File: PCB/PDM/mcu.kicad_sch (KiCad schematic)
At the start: 1 part, among them U1 STM32F405RGTx

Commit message: Fuck christmas & low side section
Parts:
- removed U1: STM32F405RGTx, Package_QFP:LQFP-64_10x10mm_P0.5mm, symbol MCU_ST_STM32F4:STM32F405RGTx
- added U1: STM32L496VGTx, Package_QFP:LQFP-100_14x14mm_P0.5mm, symbol MCU_ST_STM32L4:STM32L496VGTx
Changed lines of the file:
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@@
 (kicad_sch (version 20211123) (generator eeschema)
   (paper "A4")
-  (symbol (lib_id "MCU_ST_STM32F4:STM32F405RGTx") (at 67.945 74.93 0) (unit 1)
+  (symbol (lib_id "MCU_ST_STM32L4:STM32L496VGTx") (at 75.565 105.41 0) (unit 1)
     (in_bom yes) (on_board yes) (fields_autoplaced)
-    (property "Reference" "U1" (id 0) (at 72.5044 120.65 0)
-      (effects (font (size 0.8 0.8)) (justify left))
+    (property "Reference" "U1" (id 0) (at 85.2044 173.99 0)
+      (effects (font (size 1.27 1.27)) (justify left))
     )
-    (property "Value" "STM32F405RGTx" (id 1) (at 72.5044 123.19 0)
-      (effects (font (size 0.8 0.8)) (justify left))
+    (property "Value" "STM32L496VGTx" (id 1) (at 85.2044 176.53 0)
+      (effects (font (size 1.27 1.27)) (justify left))
     )
-    (property "Footprint" "Package_QFP:LQFP-64_10x10mm_P0.5mm" (id 2) (at 52.705 118.11 0)
+    (property "Footprint" "Package_QFP:LQFP-100_14x14mm_P0.5mm" (id 2) (at 57.785 171.45 0)
       (effects (font (size 1.27 1.27)) (justify right) hide)
     )
-    (property "Datasheet" "http://www.st.com/st-web-ui/static/active/en/resource/technical/document/datasheet/DM00037051.pdf" (id 3) (at 67.945 74.93 0)
+    (property "Datasheet" "http://www.st.com/st-web-ui/static/active/en/resource/technical/document/datasheet/DM00284211.pdf" (id 3) (at 75.565 105.41 0)
       (effects (font (size 1.27 1.27)) hide)
     )
     (pin "1")
     (pin "10")
+    (pin "100")
     (pin "11")
     (pin "12")
@@
     (pin "63")
     (pin "64")
+    (pin "65")
+    (pin "66")
+    (pin "67")
+    (pin "68")
+    (pin "69")
     (pin "7")
+    (pin "70")
+    (pin "71")
+    (pin "72")
+    (pin "73")
+    (pin "74")
+    (pin "75")
+    (pin "76")
+    (pin "77")
+    (pin "78")
+    (pin "79")
     (pin "8")
+    (pin "80")
+    (pin "81")
+    (pin "82")
+    (pin "83")
+    (pin "84")
+    (pin "85")
+    (pin "86")
+    (pin "87")
+    (pin "88")
+    (pin "89")
     (pin "9")
+    (pin "90")
+    (pin "91")
+    (pin "92")
+    (pin "93")
+    (pin "94")
+    (pin "95")
+    (pin "96")
+    (pin "97")
+    (pin "98")
+    (pin "99")
   )
 )

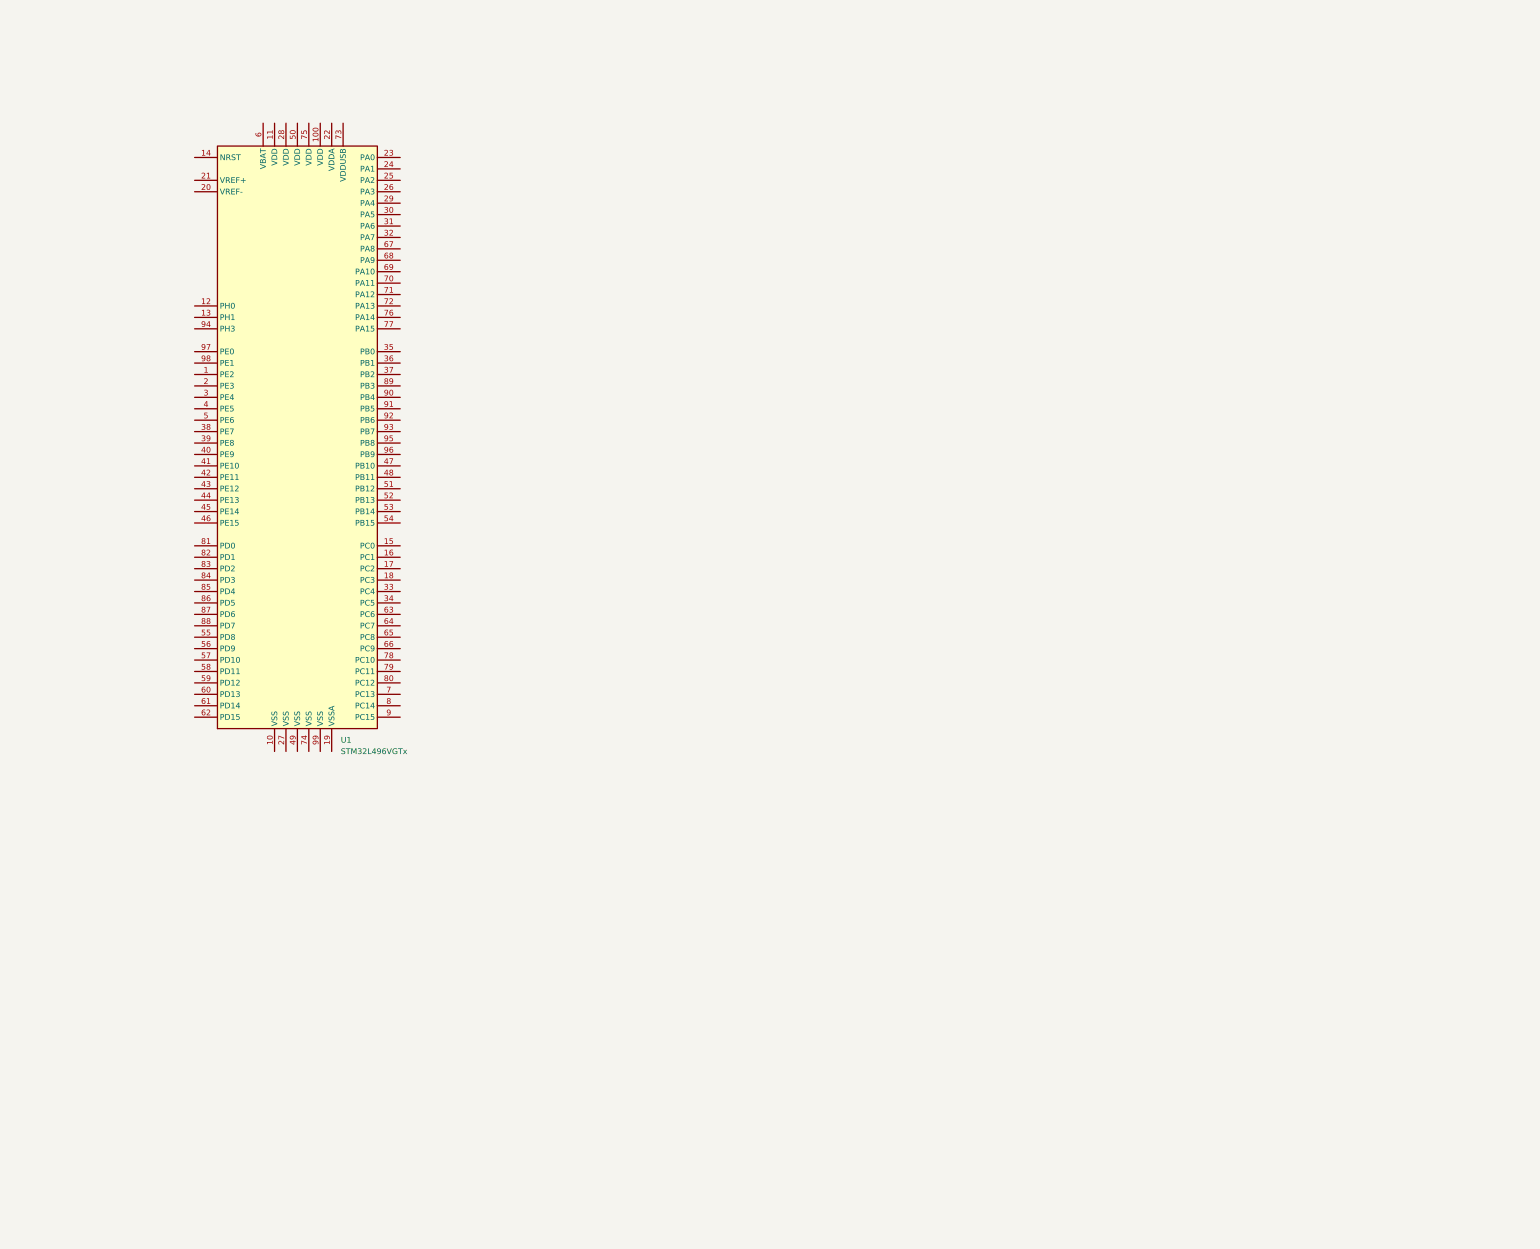
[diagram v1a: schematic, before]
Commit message: Concept revision and MCU section changes
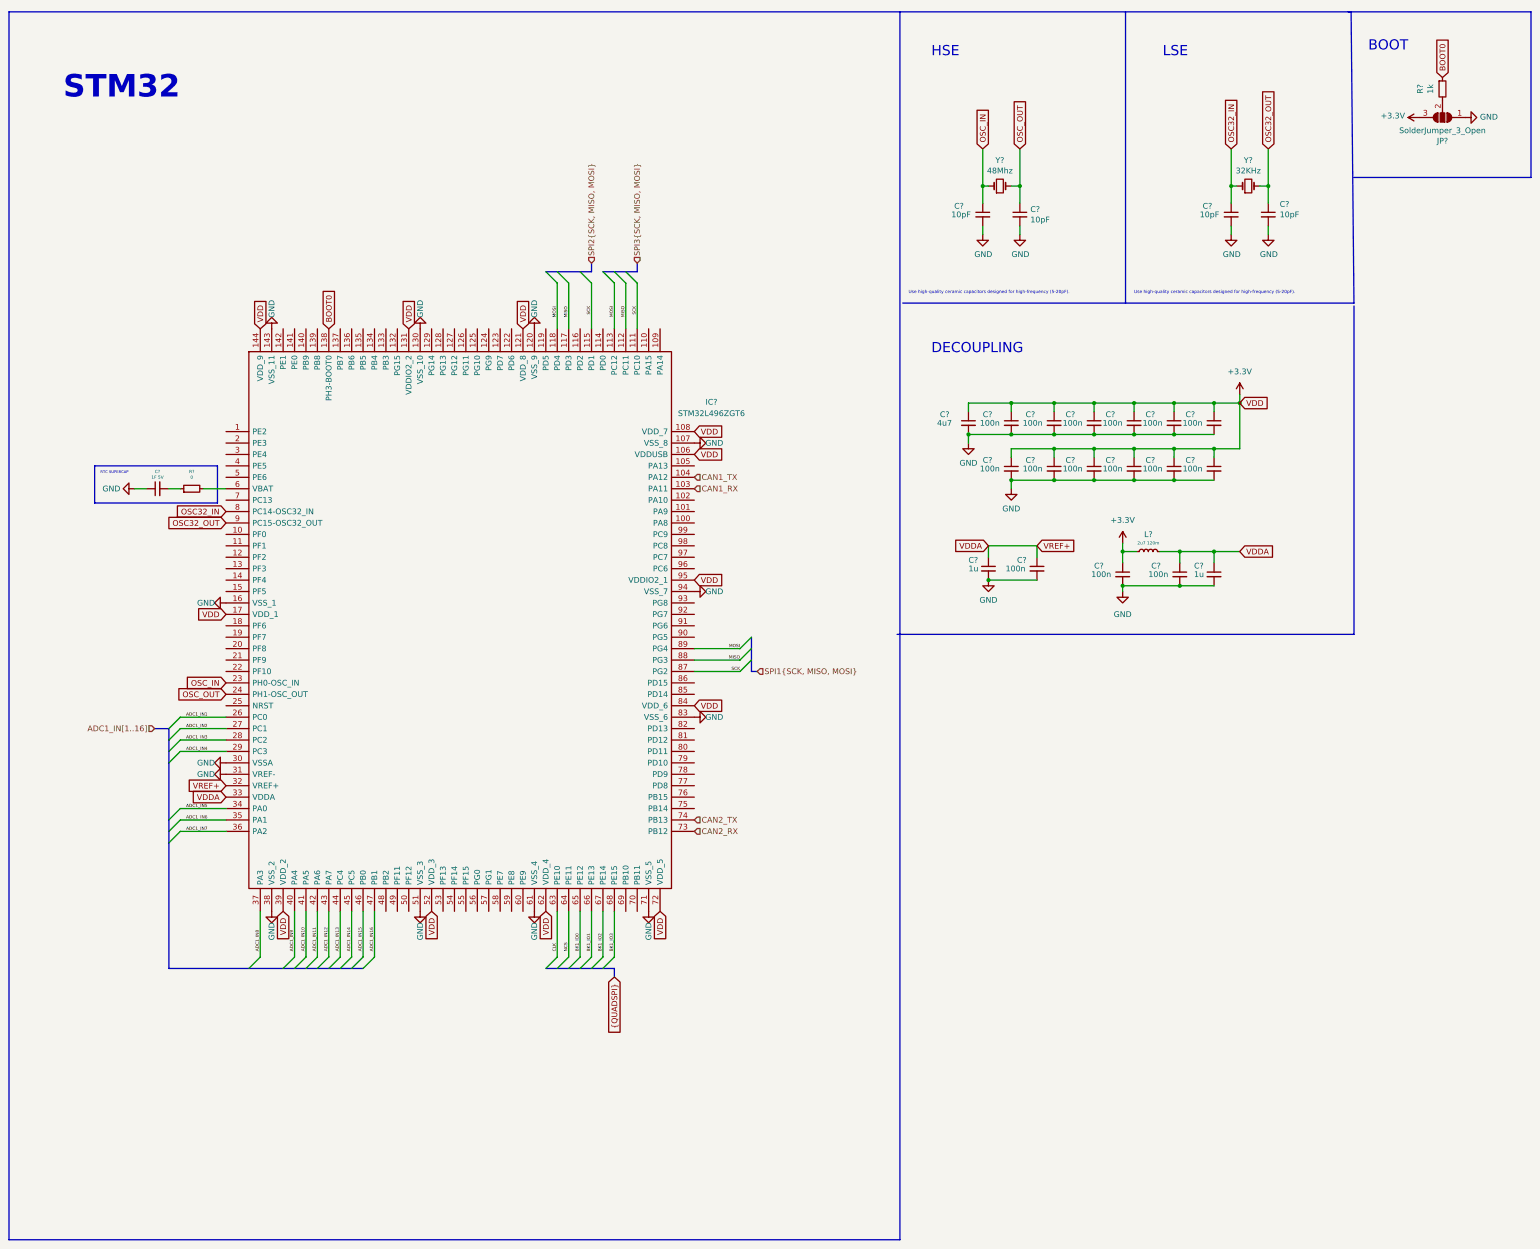
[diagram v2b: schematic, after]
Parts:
- removed U1: STM32L496VGTx, Package_QFP:LQFP-100_14x14mm_P0.5mm, symbol MCU_ST_STM32L4:STM32L496VGTx
- added C? (x15): 100n, Capacitor_SMD:C_0402_1005Metric_Pad0.74x0.62mm_HandSolder, symbol Device:C_Small
- added C? (x4): 10pF, Capacitor_SMD:C_0402_1005Metric_Pad0.74x0.62mm_HandSolder, symbol Device:C_Small
- added C? (x2): 1u, Capacitor_SMD:C_0402_1005Metric_Pad0.74x0.62mm_HandSolder, symbol Device:C_Small
- added C?: 1F 5V, symbol Device:C_Small
- added C?: 4u7, Capacitor_SMD:C_0402_1005Metric_Pad0.74x0.62mm_HandSolder, symbol Device:C_Small
- added IC?: STM32L496ZGT6, QFP50P2200X2200X160-144N, symbol PDM_additional:STM32L496ZGT6
- added JP?: SolderJumper_3_Open, Jumper:SolderJumper-3_P1.3mm_Open_RoundedPad1.0x1.5mm, symbol can2usb-rescue:SolderJumper_3_Open-Jumper
- added L?: 2u7 120m, symbol Device:L_Small
- added R?: 1k, Resistor_SMD:R_0402_1005Metric_Pad0.72x0.64mm_HandSolder, symbol Device:R_Small
- added R?: 0, symbol Device:R_Small
- added Y?: 32KHz, Crystal:Crystal_SMD_3215-2Pin_3.2x1.5mm, symbol Device:Crystal_Small
- added Y?: 48Mhz, Crystal:Crystal_SMD_5032-2Pin_5.0x3.2mm, symbol Device:Crystal_Small
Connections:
- new net: IC?.6 (VBAT), R?.2
- new net: JP?.2 (C), R?.2
- new net: C?.2, R?.1
- new net +3.3V: C?.1, C?.1, C?.1, C?.1, C?.1, C?.1, C?.1, C?.1, C?.1, C?.1, C?.1, C?.1, C?.1, C?.1, IC?.106 (VDDUSB), IC?.108 (VDD_7), IC?.121 (VDD_8), IC?.131 (VDDIO2_2), IC?.144 (VDD_9), IC?.17 (VDD_1), IC?.39 (VDD_2), IC?.52 (VDD_3), IC?.62 (VDD_4), IC?.72 (VDD_5), IC?.84 (VDD_6), IC?.95 (VDDIO2_1), L?.1
- new net +3V3: JP?.3 (B)
- new net ADC1_IN1: IC?.26 (PC0)
- new net ADC1_IN10: IC?.41 (PA5)
- new net ADC1_IN11: IC?.42 (PA6)
- new net ADC1_IN12: IC?.43 (PA7)
- new net ADC1_IN13: IC?.44 (PC4)
- new net ADC1_IN14: IC?.45 (PC5)
- new net ADC1_IN15: IC?.46 (PB0)
- new net ADC1_IN16: IC?.47 (PB1)
- new net ADC1_IN2: IC?.27 (PC1)
- new net ADC1_IN3: IC?.28 (PC2)
- new net ADC1_IN4: IC?.29 (PC3)
- new net ADC1_IN5: IC?.34 (PA0)
- new net ADC1_IN6: IC?.35 (PA1)
- new net ADC1_IN7: IC?.36 (PA2)
- new net ADC1_IN8: IC?.37 (PA3)
- new net ADC1_IN9: IC?.40 (PA4)
- new net BK1_IO0: IC?.65 (PE12)
- new net BK1_IO1: IC?.66 (PE13)
- new net BK1_IO2: IC?.67 (PE14)
- new net BK1_IO3: IC?.68 (PE15)
- new net BOOT0: IC?.138 (PH3-BOOT0), R?.1
- new net CAN1_RX: IC?.103 (PA11)
- new net CAN1_TX: IC?.104 (PA12)
- new net CAN2_RX: IC?.73 (PB12)
- new net CAN2_TX: IC?.74 (PB13)
- new net CLK: IC?.63 (PE10)
- new net GND: C?.1, C?.2, C?.2, C?.2, C?.2, C?.2, C?.2, C?.2, C?.2, C?.2, C?.2, C?.2, C?.2, C?.2, C?.2, C?.2, C?.2, C?.2, C?.2, C?.2, C?.2, C?.2, C?.2, IC?.107 (VSS_8), IC?.120 (VSS_9), IC?.130 (VSS_10), IC?.143 (VSS_11), IC?.16 (VSS_1), IC?.30 (VSSA), IC?.31 (VREF-), IC?.38 (VSS_2), IC?.51 (VSS_3), IC?.61 (VSS_4), IC?.71 (VSS_5), IC?.83 (VSS_6), IC?.94 (VSS_7), JP?.1 (A)
- new net MISO: IC?.112 (PC11), IC?.117 (PD3), IC?.88 (PG3)
- new net MOSI: IC?.113 (PC12), IC?.118 (PD4), IC?.89 (PG4)
- new net NCS: IC?.64 (PE11)
- new net OSC32_IN: C?.1, IC?.8 (PC14-OSC32_IN), Y?.1
- new net OSC32_OUT: C?.1, IC?.9 (PC15-OSC32_OUT), Y?.2
- new net OSC_IN: C?.1, IC?.23 (PH0-OSC_IN), Y?.1
- new net OSC_OUT: C?.1, IC?.24 (PH1-OSC_OUT), Y?.2
- new net SCK: IC?.111 (PC10), IC?.115 (PD1), IC?.87 (PG2)
- new net VDDA: C?.1, C?.1, C?.1, C?.1, IC?.32 (VREF+), IC?.33 (VDDA), L?.2
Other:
- note added: "BOOT"
- note added: "DECOUPLING"
- note added: "HSE"
- note added: "LSE"
- note added: "RTC SUPERCAP"
- note added: "STM32"
- note added: "Use high-quality ceramic capacitors designed for high-frequency (5-20pF)."

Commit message: MCU preliminary scheme and qspi flash
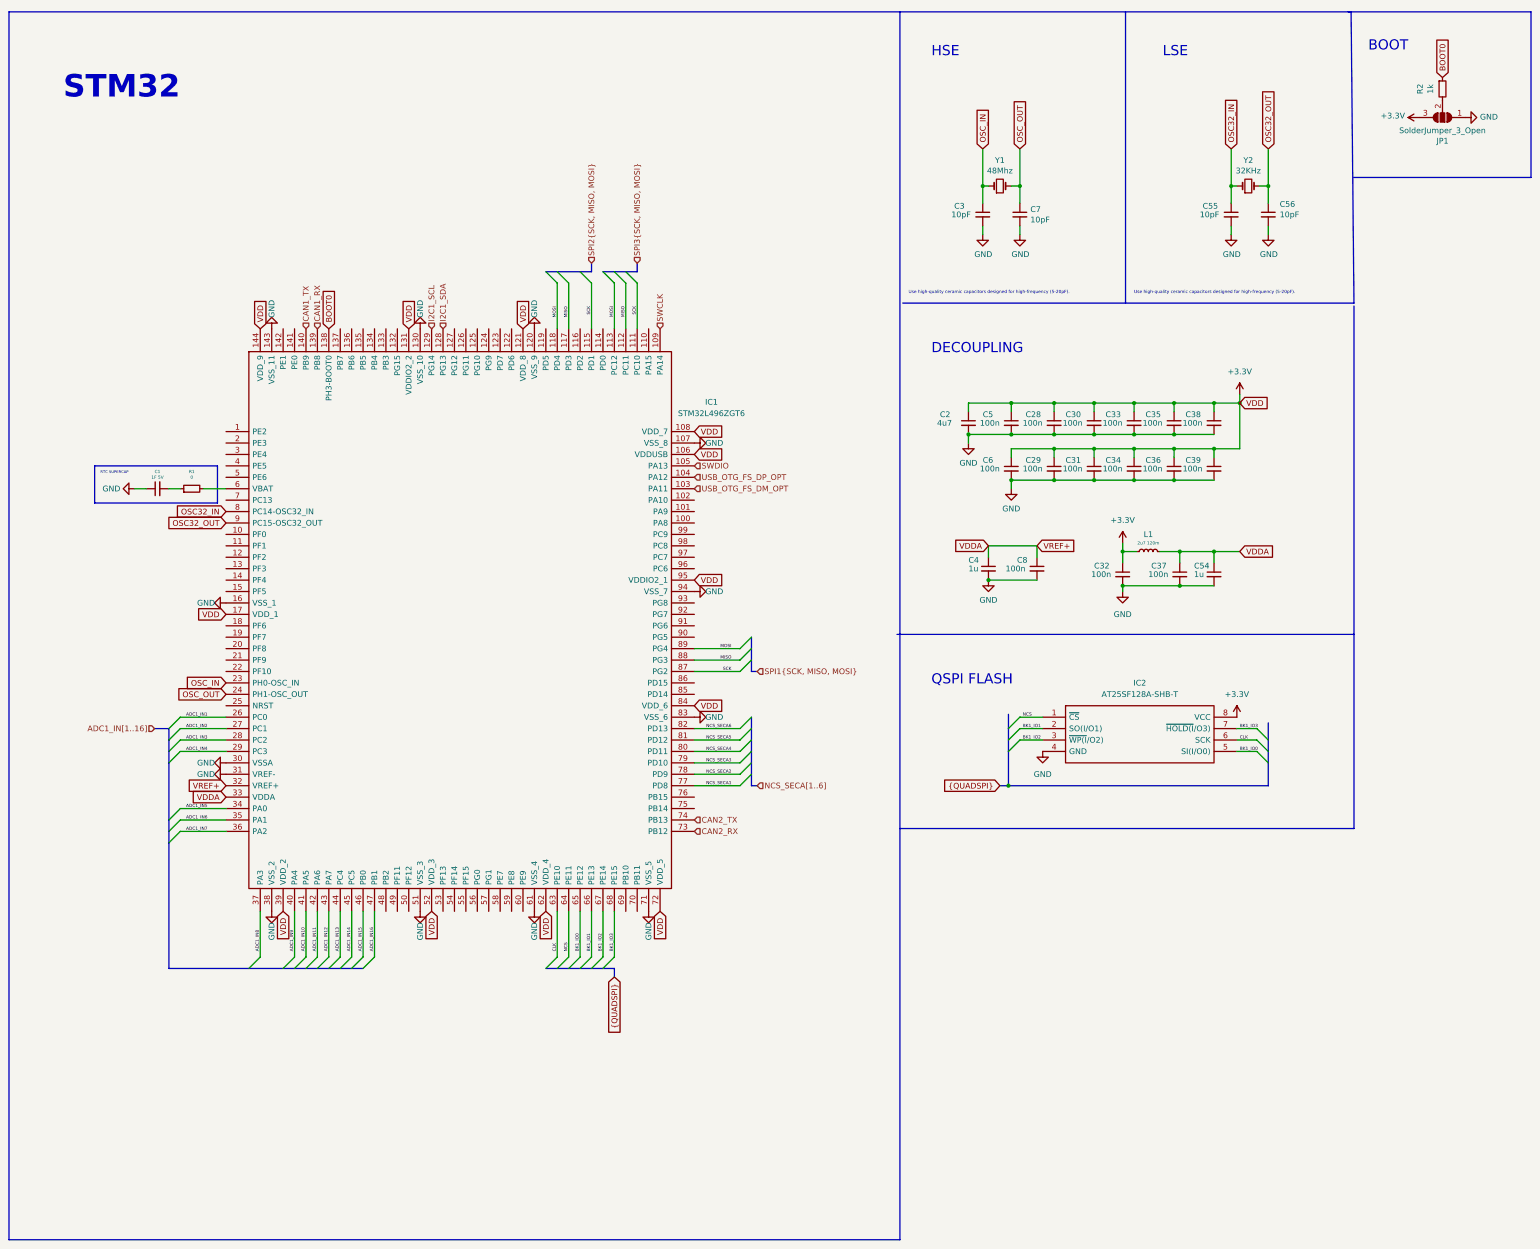
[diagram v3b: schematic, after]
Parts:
- added IC2: AT25SF128A-SHB-T, SOIC127P798X216-8N, symbol PDM_additional:AT25SF128A-SHB-T
- gave numbers to parts that had none: 30
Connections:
- net +3.3V: now also IC2.8 (VCC)
- net BK1_IO0: now also IC2.5 (SI(I/O0))
- net BK1_IO1: now also IC2.2 (SO(I/O1))
- net BK1_IO2: now also IC2.3 (~{WP(I}/O2))
- net BK1_IO3: now also IC2.7 (~{HOLD(I}/O3))
- net CAN1_RX: now also IC1.139 (PB8); no longer IC1.103 (PA11)
- net CAN1_TX: now also IC1.140 (PB9); no longer IC1.104 (PA12)
- net CLK: now also IC2.6 (SCK)
- net GND: now also IC2.4 (GND)
- net NCS: now also IC2.1 (~{CS})
- net SWDIO: now reaches IC1.105 (PA13)
- net SWCLK: now reaches IC1.109 (PA14)
- net I2C1_SDA: now reaches IC1.128 (PG13)
- net I2C1_SCL: now reaches IC1.129 (PG14)
- net NCS_SECA1: now reaches IC1.77 (PD8)
- net NCS_SECA2: now reaches IC1.78 (PD9)
- net NCS_SECA3: now reaches IC1.79 (PD10)
- net NCS_SECA4: now reaches IC1.80 (PD11)
- net NCS_SECA5: now reaches IC1.81 (PD12)
- net NCS_SECA6: now reaches IC1.82 (PD13)
- new net USB_OTG_FS_DM_OPT: IC1.103 (PA11)
- new net USB_OTG_FS_DP_OPT: IC1.104 (PA12)
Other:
- note added: "QSPI FLASH"

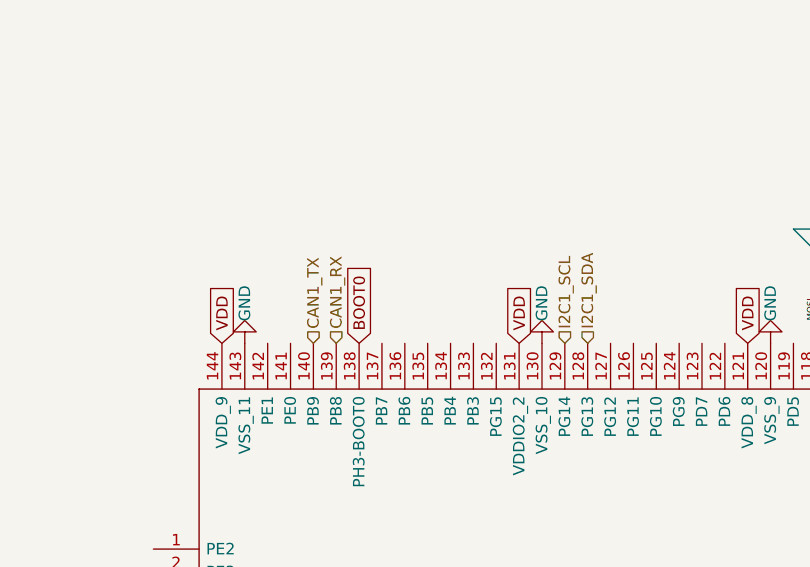
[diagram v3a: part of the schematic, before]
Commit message: Added new type of high side driver based on VNF1048 + STL135
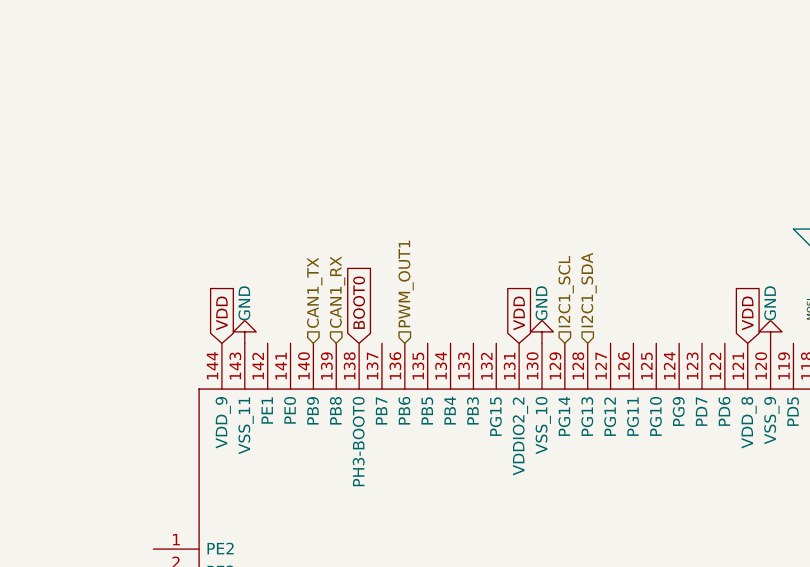
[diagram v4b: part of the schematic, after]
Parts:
- IC1: footprint QFP50P2200X2200X160-144N -> PDM_Additional:QFP50P2200X2200X160-144N
- IC2: footprint SOIC127P798X216-8N -> PDM_Additional:SOIC127P798X216-8N
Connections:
- net PWM_OUT1: now reaches IC1.136 (PB6)
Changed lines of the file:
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@@
+    (effects (font (size 1.27 1.27)) (justify left))
+  )
+  (hierarchical_label "PWM_OUT1" (shape input) (at 87.63 82.55 90)
     (effects (font (size 1.27 1.27)) (justify left))
   )
@@
     (property "Reference" "IC1" (id 0) (at 167.64 98.8312 0))
     (property "Value" "STM32L496ZGT6" (id 1) (at 167.64 101.3712 0))
-    (property "Footprint" "QFP50P2200X2200X160-144N" (id 2) (at 160.02 87.63 0)
+    (property "Footprint" "PDM_Additional:QFP50P2200X2200X160-144N" (id 2) (at 160.02 87.63 0)
       (effects (font (size 1.27 1.27)) (justify left) hide)
     )
@@
     (property "Reference" "IC2" (id 0) (at 262.89 161.29 0))
     (property "Value" "AT25SF128A-SHB-T" (id 1) (at 262.89 163.83 0))
-    (property "Footprint" "SOIC127P798X216-8N" (id 2) (at 280.67 166.37 0)
-      (effects (font (size 1.27 1.27)) (justify left) hide)
-    )
+    (property "Footprint" "PDM_Additional:SOIC127P798X216-8N" (id 2) (at 280.67 166.37 0)
+      (effects (font (size 1.27 1.27)) (justify left) hide)
+    )
